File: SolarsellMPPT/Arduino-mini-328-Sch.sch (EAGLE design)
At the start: 20 parts, among them IC1 LM358N

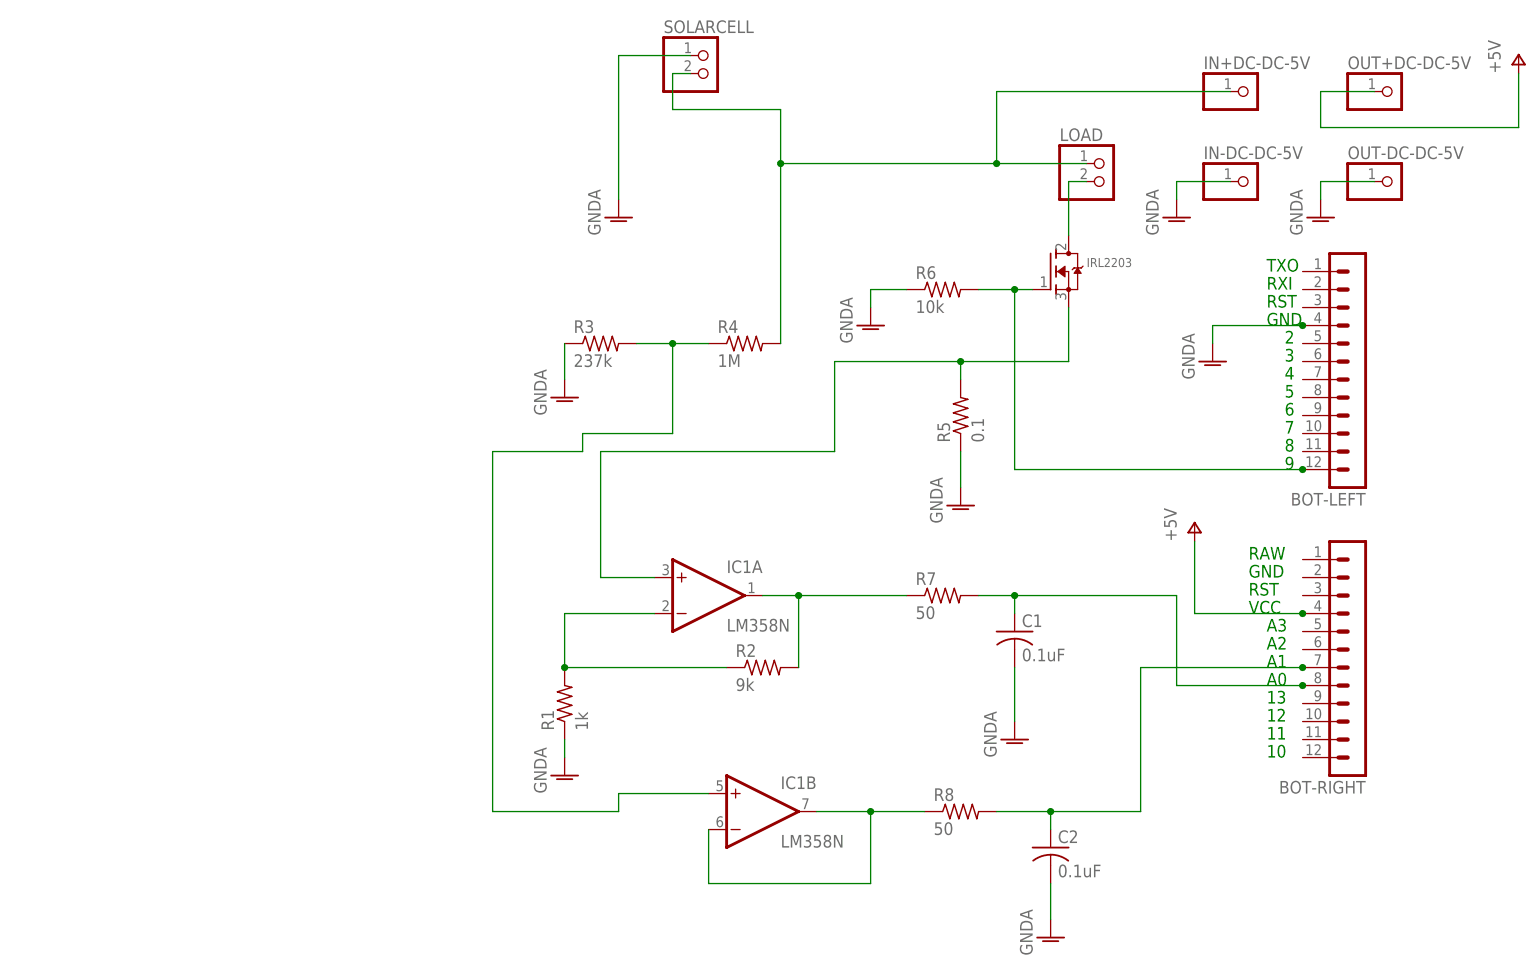
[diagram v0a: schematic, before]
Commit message: update Shc and PCB . use LM2596 to drive load
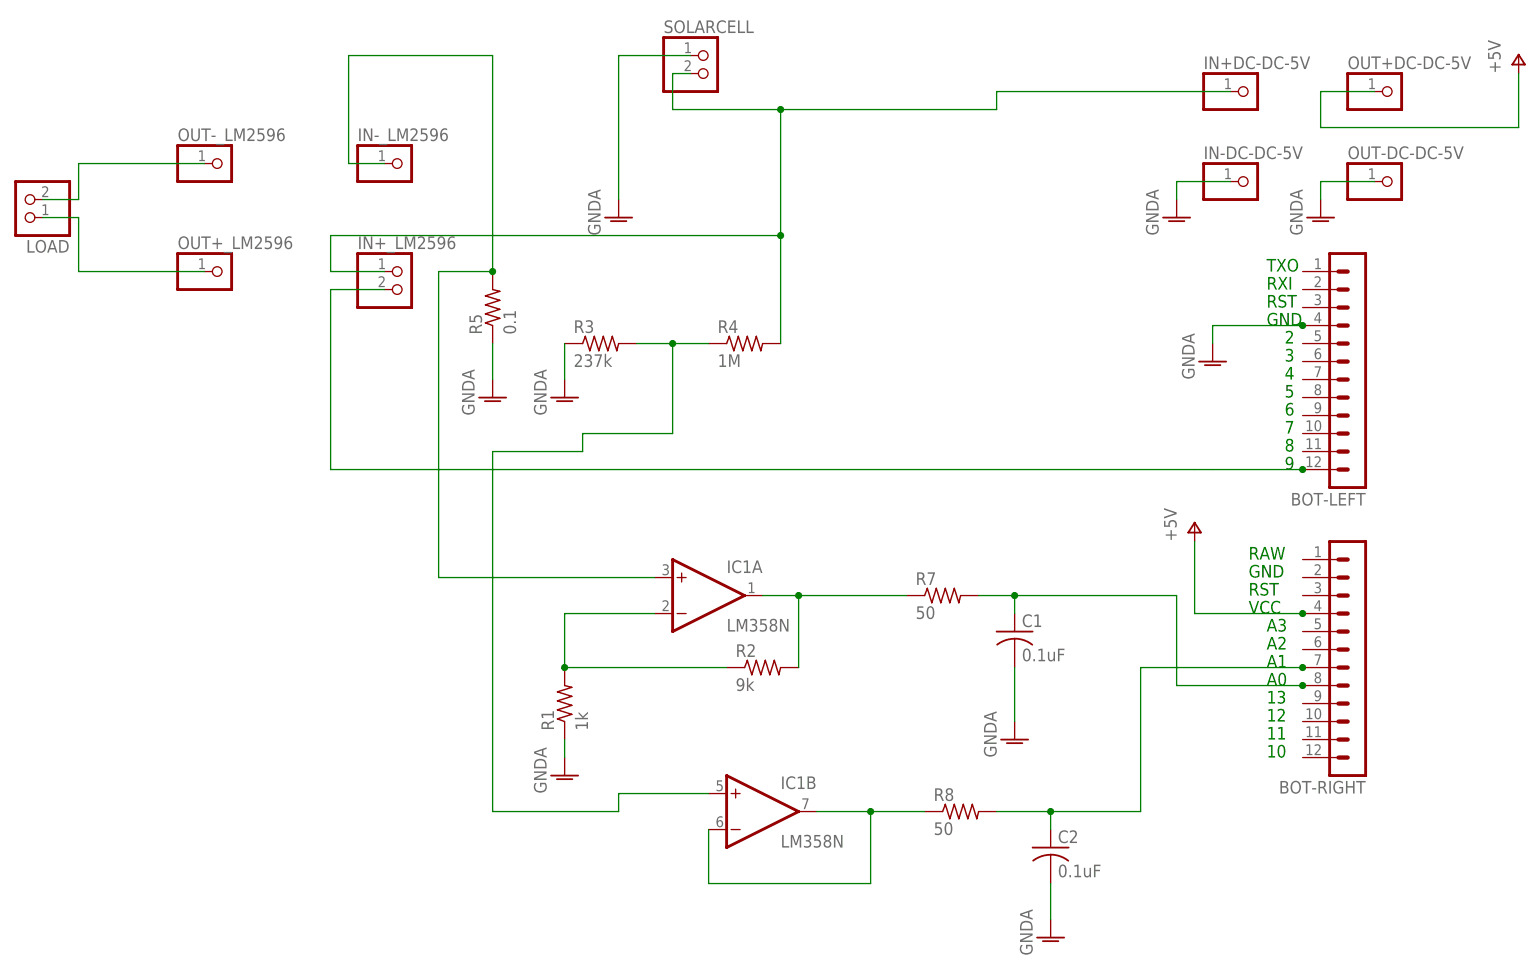
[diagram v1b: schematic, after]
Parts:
- removed IRL2203: (no value), adafruit:MOSFET-NGDS_TO220V
- removed R6: 10k, resistor:R-US_0207/10
- added IN+_LM2596: (no value), pinhead:PINHD-1X2/90
- added IN-_LM2596, OUT+_LM2596, OUT-_LM2596: (no value), pinhead:PINHD-1X1
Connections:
- removed net N$4: IC1A.+IN, IRL2203.S, R5.2
- removed net N$9: IRL2203.D, LOAD.2
- new net N$12: LOAD.2, OUT-_LM2596.1
- new net N$13: LOAD.1, OUT+_LM2596.1
- new net N$3: BOT-LEFT.12, IN+_LM2596.2
- net GNDA: no longer R6.1
- net N$10: now also IN+_LM2596.1; no longer LOAD.1
- net N$6: now also IC1A.+IN, IN-_LM2596.1, R5.2; no longer BOT-LEFT.12, IRL2203.G, R6.2
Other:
- moved on the sheet: LOAD, R5
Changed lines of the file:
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@@
 <part name="R5" library="resistor" deviceset="R-US_" device="0207/10" value="0.1"/>
 <part name="GND" library="supply1" deviceset="GNDA" device=""/>
-<part name="R6" library="resistor" deviceset="R-US_" device="0207/10" value="10k"/>
-<part name="GND1" library="supply1" deviceset="GNDA" device=""/>
 <part name="BOT-LEFT" library="con-lstb" deviceset="MA12-1" device=""/>
 <part name="BOT-RIGHT" library="con-lstb" deviceset="MA12-1" device=""/>
@@
 <part name="GND9" library="supply1" deviceset="GNDA" device=""/>
 <part name="SOLARCELL" library="pinhead" deviceset="PINHD-1X2" device=""/>
-<part name="IRL2203" library="adafruit" deviceset="MOSFET-N" device="GDS_TO220V"/>
+<part name="IN+_LM2596" library="pinhead" deviceset="PINHD-1X2" device="/90"/>
+<part name="OUT-_LM2596" library="pinhead" deviceset="PINHD-1X1" device=""/>
+<part name="IN-_LM2596" library="pinhead" deviceset="PINHD-1X1" device=""/>
+<part name="OUT+_LM2596" library="pinhead" deviceset="PINHD-1X1" device=""/>
 </parts>
 <sheets>
@@
 <instance part="R2" gate="G$1" x="33.02" y="35.56"/>
 <instance part="R4" gate="G$1" x="30.48" y="81.28"/>
-<instance part="R5" gate="G$1" x="60.96" y="71.12" rot="R90"/>
+<instance part="R5" gate="G$1" x="-5.08" y="86.36" rot="R90"/>
 <instance part="GND" gate="1" x="5.08" y="20.32"/>
-<instance part="R6" gate="G$1" x="58.42" y="88.9"/>
-<instance part="GND1" gate="1" x="48.26" y="83.82"/>
 <instance part="BOT-LEFT" gate="1" x="116.84" y="78.74" smashed="yes" rot="R180">
 <attribute name="VALUE" x="118.11" y="96.52" size="1.778" layer="96" rot="R180"/>
@@
 <instance part="C1" gate="G$1" x="68.58" y="40.64"/>
 <instance part="C2" gate="G$1" x="73.66" y="10.16"/>
-<instance part="LOAD" gate="G$1" x="81.28" y="104.14"/>
+<instance part="LOAD" gate="G$1" x="-71.12" y="101.6" rot="R180"/>
 <instance part="GND4" gate="1" x="12.7" y="99.06"/>
 <instance part="GND5" gate="1" x="5.08" y="73.66"/>
@@
 <instance part="+5V" gate="1" x="139.7" y="121.92"/>
 <instance part="+5V1" gate="1" x="93.98" y="55.88"/>
-<instance part="GND9" gate="1" x="60.96" y="58.42"/>
+<instance part="GND9" gate="1" x="-5.08" y="73.66"/>
 <instance part="SOLARCELL" gate="G$1" x="25.4" y="119.38"/>
-<instance part="IRL2203" gate="G$1" x="73.66" y="91.44"/>
+<instance part="IN+_LM2596" gate="G$1" x="-17.78" y="88.9"/>
+<instance part="OUT-_LM2596" gate="G$1" x="-43.18" y="106.68"/>
+<instance part="IN-_LM2596" gate="G$1" x="-17.78" y="106.68"/>
+<instance part="OUT+_LM2596" gate="G$1" x="-43.18" y="91.44"/>
 </instances>
 <busses>
@@
 </segment>
 <segment>
-<pinref part="GND1" gate="1" pin="GNDA"/>
-<wire x1="48.26" y1="86.36" x2="48.26" y2="88.9" width="0.1524" layer="91"/>
-<pinref part="R6" gate="G$1" pin="1"/>
-<wire x1="48.26" y1="88.9" x2="53.34" y2="88.9" width="0.1524" layer="91"/>
-</segment>
-<segment>
 <pinref part="C2" gate="G$1" pin="2"/>
 <pinref part="GND3" gate="1" pin="GNDA"/>
@@
 <segment>
 <pinref part="R5" gate="G$1" pin="1"/>
-<wire x1="60.96" y1="66.04" x2="60.96" y2="60.96" width="0.1524" layer="91"/>
+<wire x1="-5.08" y1="81.28" x2="-5.08" y2="76.2" width="0.1524" layer="91"/>
 <pinref part="GND9" gate="1" pin="GNDA"/>
 </segment>
@@
 <wire x1="93.98" y1="43.18" x2="93.98" y2="53.34" width="0.1524" layer="91"/>
 <junction x="109.22" y="43.18"/>
-</segment>
-</net>
-<net name="N$4" class="0">
-<segment>
-<pinref part="R5" gate="G$1" pin="2"/>
-<wire x1="76.2" y1="86.36" x2="76.2" y2="78.74" width="0.1524" layer="91"/>
-<wire x1="76.2" y1="78.74" x2="60.96" y2="78.74" width="0.1524" layer="91"/>
-<wire x1="60.96" y1="78.74" x2="60.96" y2="76.2" width="0.1524" layer="91"/>
-<pinref part="IRL2203" gate="G$1" pin="S"/>
-<wire x1="60.96" y1="78.74" x2="43.18" y2="78.74" width="0.1524" layer="91"/>
-<wire x1="43.18" y1="78.74" x2="43.18" y2="66.04" width="0.1524" layer="91"/>
-<wire x1="43.18" y1="66.04" x2="10.16" y2="66.04" width="0.1524" layer="91"/>
-<wire x1="10.16" y1="66.04" x2="10.16" y2="48.26" width="0.1524" layer="91"/>
-<pinref part="IC1" gate="A" pin="+IN"/>
-<wire x1="10.16" y1="48.26" x2="17.78" y2="48.26" width="0.1524" layer="91"/>
-<junction x="60.96" y="78.74"/>
 </segment>
 </net>
@@
 <wire x1="48.26" y1="15.24" x2="55.88" y2="15.24" width="0.1524" layer="91"/>
 <junction x="48.26" y="15.24"/>
-</segment>
-</net>
-<net name="N$6" class="0">
-<segment>
-<pinref part="R6" gate="G$1" pin="2"/>
-<wire x1="63.5" y1="88.9" x2="68.58" y2="88.9" width="0.1524" layer="91"/>
-<pinref part="BOT-LEFT" gate="1" pin="12"/>
-<wire x1="68.58" y1="88.9" x2="71.12" y2="88.9" width="0.1524" layer="91"/>
-<wire x1="109.22" y1="63.5" x2="68.58" y2="63.5" width="0.1524" layer="91"/>
-<wire x1="68.58" y1="63.5" x2="68.58" y2="88.9" width="0.1524" layer="91"/>
-<junction x="68.58" y="88.9"/>
-<junction x="109.22" y="63.5"/>
-<pinref part="IRL2203" gate="G$1" pin="G"/>
 </segment>
 </net>
@@
 </segment>
 </net>
-<net name="N$9" class="0">
-<segment>
-<pinref part="LOAD" gate="G$1" pin="2"/>
-<wire x1="78.74" y1="104.14" x2="76.2" y2="104.14" width="0.1524" layer="91"/>
-<wire x1="76.2" y1="104.14" x2="76.2" y2="96.52" width="0.1524" layer="91"/>
-<pinref part="IRL2203" gate="G$1" pin="D"/>
-</segment>
-</net>
 <net name="N$10" class="0">
 <segment>
 <pinref part="R4" gate="G$1" pin="2"/>
-<pinref part="LOAD" gate="G$1" pin="1"/>
-<wire x1="35.56" y1="106.68" x2="35.56" y2="81.28" width="0.1524" layer="91"/>
-<wire x1="78.74" y1="106.68" x2="66.04" y2="106.68" width="0.1524" layer="91"/>
-<junction x="35.56" y="106.68"/>
+<wire x1="35.56" y1="114.3" x2="35.56" y2="96.52" width="0.1524" layer="91"/>
+<junction x="35.56" y="114.3"/>
 <pinref part="IN+DC-DC-5V" gate="G$1" pin="1"/>
-<wire x1="66.04" y1="106.68" x2="35.56" y2="106.68" width="0.1524" layer="91"/>
+<wire x1="35.56" y1="96.52" x2="35.56" y2="81.28" width="0.1524" layer="91"/>
+<wire x1="66.04" y1="114.3" x2="35.56" y2="114.3" width="0.1524" layer="91"/>
 <wire x1="99.06" y1="116.84" x2="66.04" y2="116.84" width="0.1524" layer="91"/>
-<wire x1="66.04" y1="116.84" x2="66.04" y2="106.68" width="0.1524" layer="91"/>
-<junction x="66.04" y="106.68"/>
+<wire x1="66.04" y1="116.84" x2="66.04" y2="114.3" width="0.1524" layer="91"/>
 <pinref part="SOLARCELL" gate="G$1" pin="2"/>
 <wire x1="22.86" y1="119.38" x2="20.32" y2="119.38" width="0.1524" layer="91"/>
 <wire x1="20.32" y1="119.38" x2="20.32" y2="114.3" width="0.1524" layer="91"/>
 <wire x1="20.32" y1="114.3" x2="35.56" y2="114.3" width="0.1524" layer="91"/>
-<wire x1="35.56" y1="114.3" x2="35.56" y2="106.68" width="0.1524" layer="91"/>
+<wire x1="35.56" y1="96.52" x2="-27.94" y2="96.52" width="0.1524" layer="91"/>
+<wire x1="-27.94" y1="96.52" x2="-27.94" y2="91.44" width="0.1524" layer="91"/>
+<pinref part="IN+_LM2596" gate="G$1" pin="1"/>
+<wire x1="-27.94" y1="91.44" x2="-20.32" y2="91.44" width="0.1524" layer="91"/>
+<junction x="35.56" y="96.52"/>
 </segment>
 </net>
@@
 </segment>
 </net>
+<net name="N$3" class="0">
+<segment>
+<pinref part="BOT-LEFT" gate="1" pin="12"/>
+<wire x1="109.22" y1="63.5" x2="96.52" y2="63.5" width="0.1524" layer="91"/>
+<junction x="109.22" y="63.5"/>
+<pinref part="IN+_LM2596" gate="G$1" pin="2"/>
+<wire x1="-20.32" y1="88.9" x2="-27.94" y2="88.9" width="0.1524" layer="91"/>
+<wire x1="-27.94" y1="88.9" x2="-27.94" y2="63.5" width="0.1524" layer="91"/>
+<wire x1="-27.94" y1="63.5" x2="93.98" y2="63.5" width="0.1524" layer="91"/>
+<wire x1="96.52" y1="63.5" x2="93.98" y2="63.5" width="0.1524" layer="91"/>
+</segment>
+</net>
+<net name="N$6" class="0">
+<segment>
+<wire x1="-25.4" y1="121.92" x2="-25.4" y2="106.68" width="0.1524" layer="91"/>
+<pinref part="IN-_LM2596" gate="G$1" pin="1"/>
+<wire x1="-25.4" y1="106.68" x2="-20.32" y2="106.68" width="0.1524" layer="91"/>
+<wire x1="-5.08" y1="91.44" x2="-12.7" y2="91.44" width="0.1524" layer="91"/>
+<wire x1="-12.7" y1="91.44" x2="-12.7" y2="48.26" width="0.1524" layer="91"/>
+<pinref part="IC1" gate="A" pin="+IN"/>
+<wire x1="-12.7" y1="48.26" x2="17.78" y2="48.26" width="0.1524" layer="91"/>
+<wire x1="-25.4" y1="121.92" x2="-5.08" y2="121.92" width="0.1524" layer="91"/>
+<wire x1="-5.08" y1="121.92" x2="-5.08" y2="91.44" width="0.1524" layer="91"/>
+<pinref part="R5" gate="G$1" pin="2"/>
+<junction x="-5.08" y="91.44"/>
+</segment>
+</net>
+<net name="N$12" class="0">
+<segment>
+<pinref part="OUT-_LM2596" gate="G$1" pin="1"/>
+<wire x1="-45.72" y1="106.68" x2="-63.5" y2="106.68" width="0.1524" layer="91"/>
+<wire x1="-63.5" y1="106.68" x2="-63.5" y2="101.6" width="0.1524" layer="91"/>
+<pinref part="LOAD" gate="G$1" pin="2"/>
+<wire x1="-63.5" y1="101.6" x2="-68.58" y2="101.6" width="0.1524" layer="91"/>
+</segment>
+</net>
+<net name="N$13" class="0">
+<segment>
+<pinref part="OUT+_LM2596" gate="G$1" pin="1"/>
+<wire x1="-63.5" y1="91.44" x2="-45.72" y2="91.44" width="0.1524" layer="91"/>
+<pinref part="LOAD" gate="G$1" pin="1"/>
+<wire x1="-68.58" y1="99.06" x2="-63.5" y2="99.06" width="0.1524" layer="91"/>
+<wire x1="-63.5" y1="99.06" x2="-63.5" y2="91.44" width="0.1524" layer="91"/>
+</segment>
+</net>
